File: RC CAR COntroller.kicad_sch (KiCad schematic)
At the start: 17 parts, among them J101 USB_C_14P_2.0, J102 Conn_01x03, J103 Conn_ST_STDC14, SW101 SW_Push, U101 USBLC6-2SC6, U102 STM32F303CCTx, Y101 16MHz

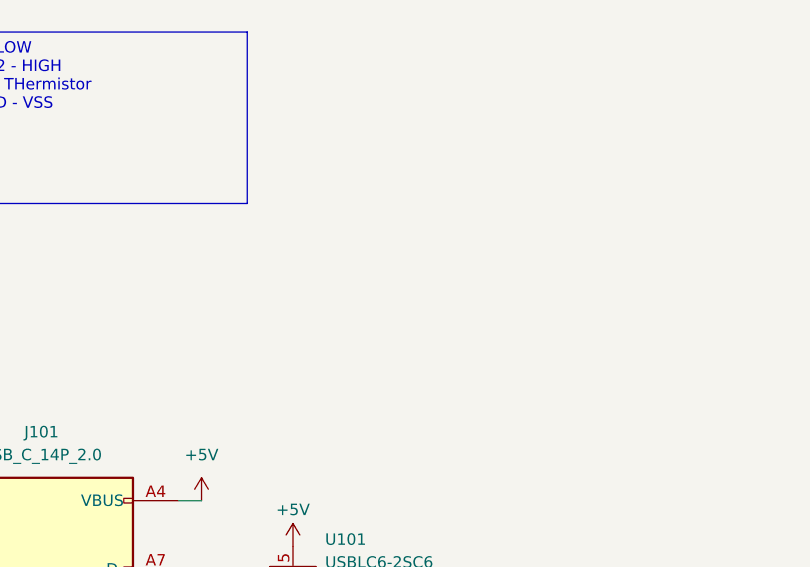
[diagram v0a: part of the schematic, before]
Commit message: added resistr test
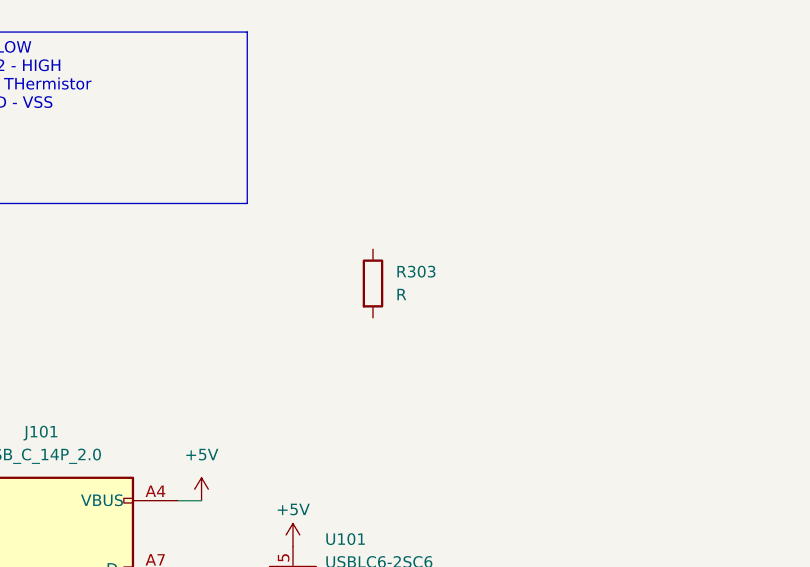
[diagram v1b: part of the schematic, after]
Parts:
- added R303: R, symbol Device:R
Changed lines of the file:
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@@
+	)
+	(symbol
+		(lib_id "Device:R")
+		(at 77.47 45.72 0)
+		(unit 1)
+		(exclude_from_sim no)
+		(in_bom yes)
+		(on_board yes)
+		(dnp no)
+		(fields_autoplaced yes)
+		(property "Reference" "R303"
+			(at 80.01 44.4499 0)
+			(effects
+				(font
+					(size 1.27 1.27)
+				)
+				(justify left)
+			)
+		)
+		(property "Value" "R"
+			(at 80.01 46.9899 0)
+			(effects
+				(font
+					(size 1.27 1.27)
+				)
+				(justify left)
+			)
+		)
+		(property "Footprint" ""
+			(at 75.692 45.72 90)
+			(effects
+				(font
+					(size 1.27 1.27)
+				)
+				(hide yes)
+			)
+		)
+		(property "Datasheet" "~"
+			(at 77.47 45.72 0)
+			(effects
+				(font
+					(size 1.27 1.27)
+				)
+				(hide yes)
+			)
+		)
+		(property "Description" "Resistor"
+			(at 77.47 45.72 0)
+			(effects
+				(font
+					(size 1.27 1.27)
+				)
+				(hide yes)
+			)
+		)
+		(pin "1"
+		)
+		(pin "2"
+		)
+		(instances
+			(project ""
+				(path "/dd3da271-7a0d-4137-afa8-fed08148c503"
+					(reference "R303")
+					(unit 1)
+				)
+			)
+		)
 	)
 	(symbol

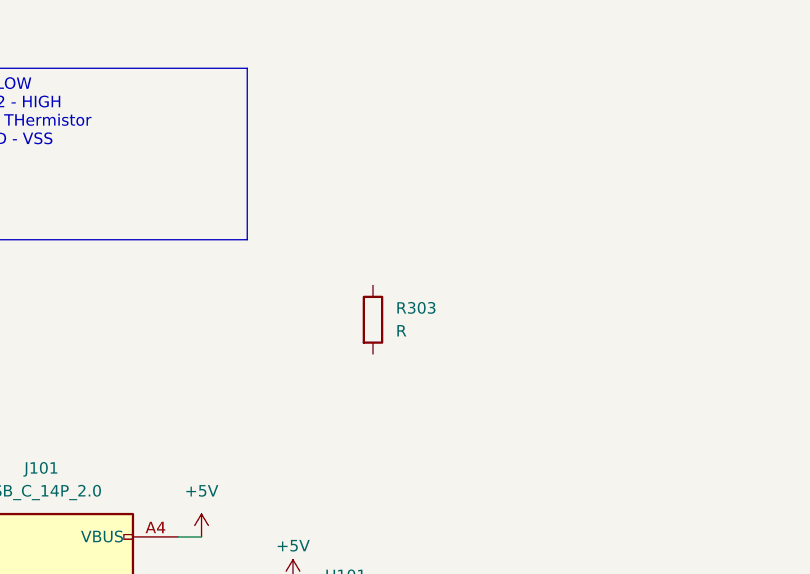
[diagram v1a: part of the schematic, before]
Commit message: added led diode test
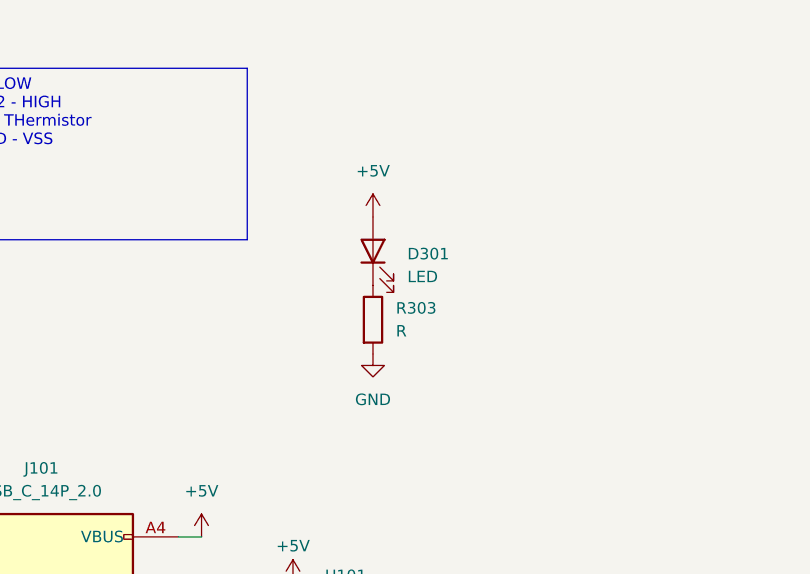
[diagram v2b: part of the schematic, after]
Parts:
- added D301: LED, symbol Device:LED
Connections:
- net +5V: now also D301.2 (A)
- net GND: now also R303.2
- net at R303.1: now also D301.1 (K)
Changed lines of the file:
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@@
+	)
+	(symbol
+		(lib_id "power:GND")
+		(at 77.47 49.53 0)
+		(unit 1)
+		(exclude_from_sim no)
+		(in_bom yes)
+		(on_board yes)
+		(dnp no)
+		(fields_autoplaced yes)
+		(property "Reference" "#PWR0155"
+			(at 77.47 55.88 0)
+			(effects
+				(font
+					(size 1.27 1.27)
+				)
+				(hide yes)
+			)
+		)
+		(property "Value" "GND"
+			(at 77.47 54.61 0)
+			(effects
+				(font
+					(size 1.27 1.27)
+				)
+			)
+		)
+		(property "Footprint" ""
+			(at 77.47 49.53 0)
+			(effects
+				(font
+					(size 1.27 1.27)
+				)
+				(hide yes)
+			)
+		)
+		(property "Datasheet" ""
+			(at 77.47 49.53 0)
+			(effects
+				(font
+					(size 1.27 1.27)
+				)
+				(hide yes)
+			)
+		)
+		(property "Description" "Power symbol creates a global label with name \"GND\" , ground"
+			(at 77.47 49.53 0)
+			(effects
+				(font
+					(size 1.27 1.27)
+				)
+				(hide yes)
+			)
+		)
+		(pin "1"
+		)
+		(instances
+			(project "RC CAR COntroller"
+				(path "/dd3da271-7a0d-4137-afa8-fed08148c503"
+					(reference "#PWR0155")
+					(unit 1)
+				)
+			)
+		)
 	)
 	(symbol
@@
 	)
 	(symbol
+		(lib_id "Device:LED")
+		(at 77.47 38.1 90)
+		(unit 1)
+		(exclude_from_sim no)
+		(in_bom yes)
+		(on_board yes)
+		(dnp no)
+		(fields_autoplaced yes)
+		(property "Reference" "D301"
+			(at 81.28 38.4174 90)
+			(effects
+				(font
+					(size 1.27 1.27)
+				)
+				(justify right)
+			)
+		)
+		(property "Value" "LED"
+			(at 81.28 40.9574 90)
+			(effects
+				(font
+					(size 1.27 1.27)
+				)
+				(justify right)
+			)
+		)
+		(property "Footprint" ""
+			(at 77.47 38.1 0)
+			(effects
+				(font
+					(size 1.27 1.27)
+				)
+				(hide yes)
+			)
+		)
+		(property "Datasheet" "~"
+			(at 77.47 38.1 0)
+			(effects
+				(font
+					(size 1.27 1.27)
+				)
+				(hide yes)
+			)
+		)
+		(property "Description" "Light emitting diode"
+			(at 77.47 38.1 0)
+			(effects
+				(font
+					(size 1.27 1.27)
+				)
+				(hide yes)
+			)
+		)
+		(property "Sim.Pins" "1=K 2=A"
+			(at 77.47 38.1 0)
+			(effects
+				(font
+					(size 1.27 1.27)
+				)
+				(hide yes)
+			)
+		)
+		(pin "2"
+		)
+		(pin "1"
+		)
+		(instances
+			(project ""
+				(path "/dd3da271-7a0d-4137-afa8-fed08148c503"
+					(reference "D301")
+					(unit 1)
+				)
+			)
+		)
+	)
+	(symbol
 		(lib_id "Switch:SW_Push")
 		(at 260.35 59.69 0)
@@
 					(unit 1)
 				)
+			)
+		)
+	)
+	(symbol
+		(lib_id "power:+5V")
+		(at 77.47 34.29 0)
+		(unit 1)
+		(exclude_from_sim no)
+		(in_bom yes)
+		(on_board yes)
+		(dnp no)
+		(fields_autoplaced yes)
+		(property "Reference" "#PWR0154"
+			(at 77.47 38.1 0)
+			(effects
+				(font
+					(size 1.27 1.27)
+				)
+				(hide yes)
+			)
+		)
+		(property "Value" "+5V"
+			(at 77.47 29.21 0)
+			(effects
+				(font
+					(size 1.27 1.27)
+				)
+			)
+		)
+		(property "Footprint" ""
+			(at 77.47 34.29 0)
+			(effects
+				(font
+					(size 1.27 1.27)
+				)
+				(hide yes)
+			)
+		)
+		(property "Datasheet" ""
+			(at 77.47 34.29 0)
+			(effects
+				(font
+					(size 1.27 1.27)
+				)
+				(hide yes)
+			)
+		)
+		(property "Description" "Power symbol creates a global label with name \"+5V\""
+			(at 77.47 34.29 0)
+			(effects
+				(font
+					(size 1.27 1.27)
+				)
+				(hide yes)
+			)
+		)
+		(pin "1"
+		)
+		(instances
+			(project "RC CAR COntroller"
+				(path "/dd3da271-7a0d-4137-afa8-fed08148c503"
+					(reference "#PWR0154")
+					(unit 1)
+				)

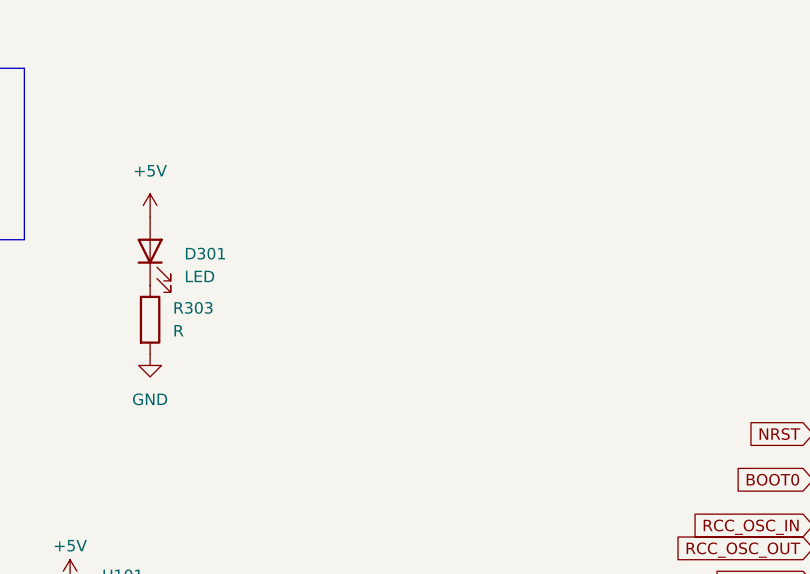
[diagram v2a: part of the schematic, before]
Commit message: added more led test
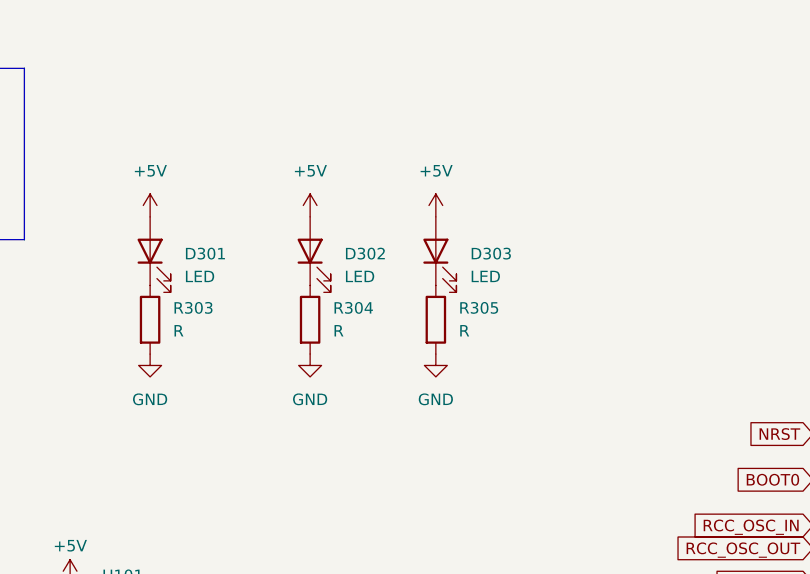
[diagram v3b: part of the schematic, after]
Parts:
- added D302, D303: LED, symbol Device:LED
- added R304, R305: R, symbol Device:R
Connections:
- net +5V: now also D302.2 (A), D303.2 (A)
- net GND: now also R304.2, R305.2
- new net: D302.1 (K), R304.1
- new net: D303.1 (K), R305.1
